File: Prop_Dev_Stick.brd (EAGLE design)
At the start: 63.2 x 24.9 mm, 55 parts, among them J1 MF-CON-MICROUSB-RIGHT, J3 M20-7822046, J4 M20-7822046, J5 M20-7820442, J6 M20-7820442, U1 P8X32A-Q44, U2 FT230XQ-R, U3 TPS2113ADRBR, U4 CAT24C512WI-GT3, U5 MAX11613EUA+, U6 NCP1117LPST33T3G, U7 IRLML6401TRPBF, X1 ABMM-6.000MHZ-B2-T

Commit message: Updated design to use latest library style!
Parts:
- removed J6: M20-7820442, PP_Connectors:HEADER_01X04_PTH_ROUND
- added J2: (no value), PP_Connectors:2.54MM_01X04_PIN_HEADER
- J1: device MF_Connectors:MICROUSB-RIGHT -> PP_Connectors:10118193-0001LF
- J3: value M20-7822046 -> (none); device PP_Connectors:HEADER_01X20_PTH_ROUND -> PP_Connectors:2.54MM_01X04_PIN_HEADER
- J4: device PP_Connectors:HEADER_01X20_PTH_ROUND -> PP_Connectors:2.54MM_01X20_PIN_HEADER
- J5: value M20-7820442 -> M20-7822046; device PP_Connectors:HEADER_01X04_PTH_ROUND -> PP_Connectors:2.54MM_01X20_PIN_HEADER
- U1: device PP_DigitalIC:LQFP-44 -> PP_DigitalIC:P8X32A_LQFP-44
- U2: device PP_DigitalIC:QFN-16 -> PP_DigitalIC:FT230X_QFN-16
- U3: device PP_PowerIC:SON-8 -> PP_PowerIC:TPS211X_SON-8
- U5: device PP_AnalogIC:UMAX-8 -> PP_AnalogIC:MAX11613_UMAX-8
- U7: device PP_DiscreteSemi:SOT-23 -> PP_DiscreteSemi:SOT-23-3
- moved J3 40.2 mm to (58.2, 23.9)
- moved J5 33.0 mm to (25.1, 23.9)
- moved J4 22.9 mm to (25.1, 1.02)
- moved J1 1.27 mm to (1.52, 12.4)
- turned U4 to 0 degrees
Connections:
- net 3.3V: now also J2.2, J3.2, J5.3; no longer J3.3, J5.2, J6.2
- net A0: now also J2.3; no longer J6.3
- net A1: now also J2.4; no longer J6.4
- net A2: now also J3.3; no longer J5.3
- net A3: now also J3.4; no longer J5.4
- net GND: now also J2.1, J3.1, J5.4, U3.PAD, U4.1; no longer J1.S5, J1.S6, J3.4, J5.1, J6.1
- net P10: now also J4.15; no longer J3.15
- net P11: now also J4.16; no longer J3.16
- net P12: now also J4.17; no longer J3.17
- net P13: now also J4.18; no longer J3.18
- net P14: now also J4.19; no longer J3.19
- net P15: now also J4.20; no longer J3.20
- net P16: now also J5.20; no longer J4.20
- net P17: now also J5.19; no longer J4.19
- net P18: now also J5.18; no longer J4.18
- net P19: now also J5.17; no longer J4.17
- net P20: now also J5.16; no longer J4.16
- net P21: now also J5.15; no longer J4.15
- net P22: now also J5.14; no longer J4.14
- net P23: now also J5.13; no longer J4.13
- net P24: now also J5.12; no longer J4.12
- net P25: now also J5.11; no longer J4.11
- net P26: now also J5.10; no longer J4.10
- net P27: now also J5.9; no longer J4.9
- net P4: now also J4.9; no longer J3.9
- net P5: now also J4.10; no longer J3.10
- net P6: now also J4.11; no longer J3.11
- net P7: now also J4.12; no longer J3.12
- net P8: now also J4.13; no longer J3.13
- net P9: now also J4.14; no longer J3.14
- net RX: now also J5.6; no longer J4.6
- net SCL: now also J5.8; no longer J4.8
- net SDA: now also J5.7; no longer J4.7
- net SD_CS: now also J4.5; no longer J3.5
- net SD_DI: now also J4.6; no longer J3.6
- net SD_DO: now also J4.8; no longer J3.8
- net SD_SCLK: now also J4.7; no longer J3.7
- net TX: now also J5.5; no longer J4.5
- net VBUS_P2: now also J5.2; no longer J3.2
- net VIN: now also J5.1; no longer J3.1
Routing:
- net GND: track 7.92 -> 10.3 mm, vias 36 -> 35
- net VBUS_P2: track 50.1 -> 49.0 mm
- net 3.3V: track 209.7 -> 210.2 mm
- net VIN: track 50.1 -> 49.6 mm

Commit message: REV 4B
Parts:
- J1: device PP_Connectors:10118193-0001LF -> MF_Connectors:MICROUSB-RIGHT
- moved J1 1.27 mm to (2.79, 12.4)
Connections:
- net GND: now also J1.S5, J1.S6
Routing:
- net GND: track 10.3 -> 18.9 mm
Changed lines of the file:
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@@
 <layer number="122" name="_bsilk" color="7" fill="1" visible="no" active="yes"/>
 <layer number="125" name="_tNames" color="7" fill="1" visible="no" active="yes"/>
+<layer number="128" name="128bmp" color="1" fill="10" visible="yes" active="yes"/>
+<layer number="129" name="129bmp" color="2" fill="4" visible="yes" active="yes"/>
+<layer number="130" name="130bmp" color="2" fill="1" visible="yes" active="yes"/>
 <layer number="131" name="prix" color="7" fill="1" visible="yes" active="yes"/>
 <layer number="132" name="test" color="7" fill="1" visible="yes" active="yes"/>
@@
 <attribute name="NAME" x="47.25225" y="19.807" size="0.8128" layer="21" font="vector"/>
 </element>
-<element name="J1" library="PP_Connectors" package="10118193-0001LF" value="MF-CON-MICROUSB-RIGHT" x="1.524" y="12.446" smashed="yes" rot="R270">
-<attribute name="NAME" x="0.635" y="17.686" size="0.8128" layer="25" font="vector"/>
-</element>
 <element name="X1" library="MF_Frequency_Control" package="7MMX5MM" value="ABMM-6.000MHZ-B2-T" x="28.829" y="18.923" smashed="yes" rot="MR0">
 <attribute name="NAME" x="32.429" y="21.923" size="0.8128" layer="26" font="vector" rot="MR0"/>
@@
 <attribute name="LABEL04" value="" x="61.976" y="-1.524" size="0.8128" layer="21" font="vector" ratio="16" rot="R90" align="center-right"/>
 <attribute name="LABEL01" value="" x="54.356" y="-1.524" size="0.8128" layer="21" font="vector" ratio="16" rot="R90" align="center-right"/>
-<attribute name="NAME" x="51.562" y="1.8415" size="0.8128" layer="21" font="vector" ratio="16"/>
 </element>
 <element name="J3" library="PP_Connectors" package="2.54MM_01X04_PIN_HEADER" value="" x="58.166" y="23.876" smashed="yes">
@@
 <attribute name="LABEL04" value="" x="61.976" y="21.336" size="0.8128" layer="21" font="vector" ratio="16" rot="R90" align="center-right"/>
 <attribute name="LABEL01" value="" x="54.356" y="21.336" size="0.8128" layer="21" font="vector" ratio="16" rot="R90" align="center-right"/>
-<attribute name="NAME" x="51.308" y="22.4155" size="0.8128" layer="21" font="vector" ratio="16"/>
 </element>
 <element name="J4" library="PP_Connectors" package="2.54MM_01X20_PIN_HEADER" value="M20-7822046" x="25.146" y="1.016" smashed="yes">
@@
 <attribute name="LABEL01" value="" x="1.016" y="-1.524" size="0.8128" layer="21" font="vector" ratio="16" rot="R90" align="center-right"/>
 <attribute name="LABEL02" value="" x="3.556" y="-1.524" size="0.8128" layer="21" font="vector" ratio="16" rot="R90" align="center-right"/>
-<attribute name="NAME" x="39.624" y="3.3655" size="0.8128" layer="21" font="vector" ratio="16"/>
 </element>
 <element name="J5" library="PP_Connectors" package="2.54MM_01X20_PIN_HEADER" value="M20-7822046" x="25.146" y="23.876" smashed="yes">
@@
 <attribute name="LABEL01" value="" x="1.016" y="21.336" size="0.8128" layer="21" font="vector" ratio="16" rot="R90" align="center-right"/>
 <attribute name="LABEL02" value="" x="3.556" y="21.336" size="0.8128" layer="21" font="vector" ratio="16" rot="R90" align="center-right"/>
-<attribute name="NAME" x="22.606" y="20.3835" size="0.8128" layer="21" font="vector" ratio="16"/>
+</element>
+<element name="J1" library="MF_Connectors" package="MICROUSB-RIGHT" value="MF-CON-MICROUSB-RIGHT" x="2.794" y="12.446" smashed="yes" rot="R270">
+<attribute name="NAME" x="0.67" y="17.686" size="0.8128" layer="25" font="vector"/>
 </element>
 </elements>
@@
 <via x="52.07" y="7.112" extent="1-16" drill="0.5"/>
 <via x="52.07" y="5.588" extent="1-16" drill="0.5"/>
-<contactref element="J1" pad="5"/>
-<contactref element="J1" pad="5"/>
-<contactref element="J1" pad="S1"/>
-<contactref element="J1" pad="S4"/>
-<contactref element="J1" pad="S3"/>
-<contactref element="J1" pad="S2"/>
 <via x="18.288" y="14.478" extent="1-16" drill="0.5"/>
 <via x="23.622" y="18.034" extent="1-16" drill="0.5"/>
@@
 <contactref element="J4" pad="4"/>
 <contactref element="J5" pad="4"/>
+<contactref element="J1" pad="5"/>
+<contactref element="J1" pad="S1"/>
+<contactref element="J1" pad="S3"/>
+<contactref element="J1" pad="S5"/>
+<contactref element="J1" pad="S2"/>
+<contactref element="J1" pad="S4"/>
+<contactref element="J1" pad="S6"/>
+<wire x1="1.389" y1="13.646" x2="1.27" y2="13.646" width="0.6096" layer="1"/>
+<wire x1="1.27" y1="13.646" x2="1.27" y2="15.746" width="0.6096" layer="1"/>
+<wire x1="1.27" y1="15.746" x2="1.27" y2="17.018" width="0.6096" layer="1"/>
+<wire x1="1.389" y1="11.246" x2="1.27" y2="11.246" width="0.6096" layer="1"/>
+<wire x1="1.27" y1="11.246" x2="1.27" y2="9.146" width="0.6096" layer="1"/>
+<wire x1="1.27" y1="7.874" x2="1.394" y2="7.874" width="0.6096" layer="1"/>
+<wire x1="1.394" y1="7.874" x2="1.394" y2="9.146" width="0.6096" layer="1"/>
+<wire x1="1.394" y1="15.746" x2="1.27" y2="15.746" width="0.6096" layer="1"/>
+<wire x1="1.394" y1="9.146" x2="1.27" y2="9.146" width="0.6096" layer="1"/>
+<wire x1="1.27" y1="9.146" x2="1.27" y2="7.874" width="0.6096" layer="1"/>
 </signal>
 <signal name="SDA">
@@
 <signal name="VBUS">
 <contactref element="L1" pad="1"/>
-<contactref element="J1" pad="1"/>
-<wire x1="4.064" y1="13.746" x2="4.856" y2="13.746" width="0.254" layer="1"/>
 <wire x1="4.856" y1="13.746" x2="5.969" y2="14.859" width="0.254" layer="1"/>
 <wire x1="5.969" y1="14.859" x2="6.008" y2="14.859" width="0.254" layer="1"/>
+<contactref element="J1" pad="1"/>
+<wire x1="4.856" y1="13.746" x2="4.064" y2="13.746" width="0.254" layer="1"/>
 </signal>
 <signal name="D+">
@@
 <wire x1="5.246" y1="12.446" x2="6.008" y2="11.684" width="0.254" layer="1"/>
 <contactref element="J1" pad="3"/>
-<wire x1="4.064" y1="12.446" x2="5.246" y2="12.446" width="0.254" layer="1"/>
+<wire x1="5.246" y1="12.446" x2="4.064" y2="12.446" width="0.254" layer="1"/>
 </signal>
 <signal name="RX">
@@
 <contactref element="R13" pad="2"/>
 <wire x1="6.008" y1="12.969" x2="6.008" y2="13.208" width="0.254" layer="1"/>
+<wire x1="5.896" y1="13.096" x2="6.008" y2="13.208" width="0.254" layer="1"/>
 <contactref element="J1" pad="2"/>
-<wire x1="4.064" y1="13.096" x2="5.896" y2="13.096" width="0.254" layer="1"/>
-<wire x1="5.896" y1="13.096" x2="6.008" y2="13.208" width="0.254" layer="1"/>
+<wire x1="5.896" y1="13.096" x2="4.064" y2="13.096" width="0.254" layer="1"/>
 </signal>
 <signal name="5V">

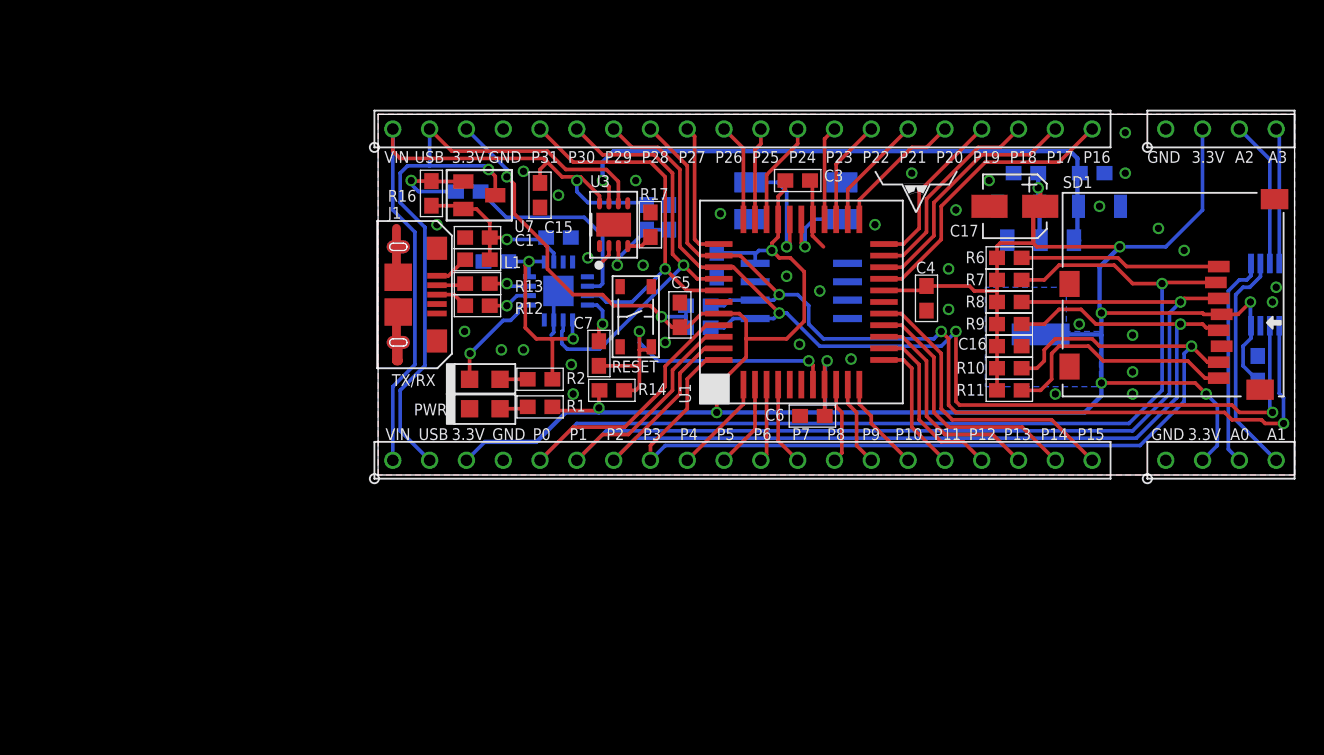
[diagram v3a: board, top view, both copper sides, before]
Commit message: Working on REV5
REV5 will feature 0402 parts, QFN Prop, USB Type-C, and a host of other
small changes.
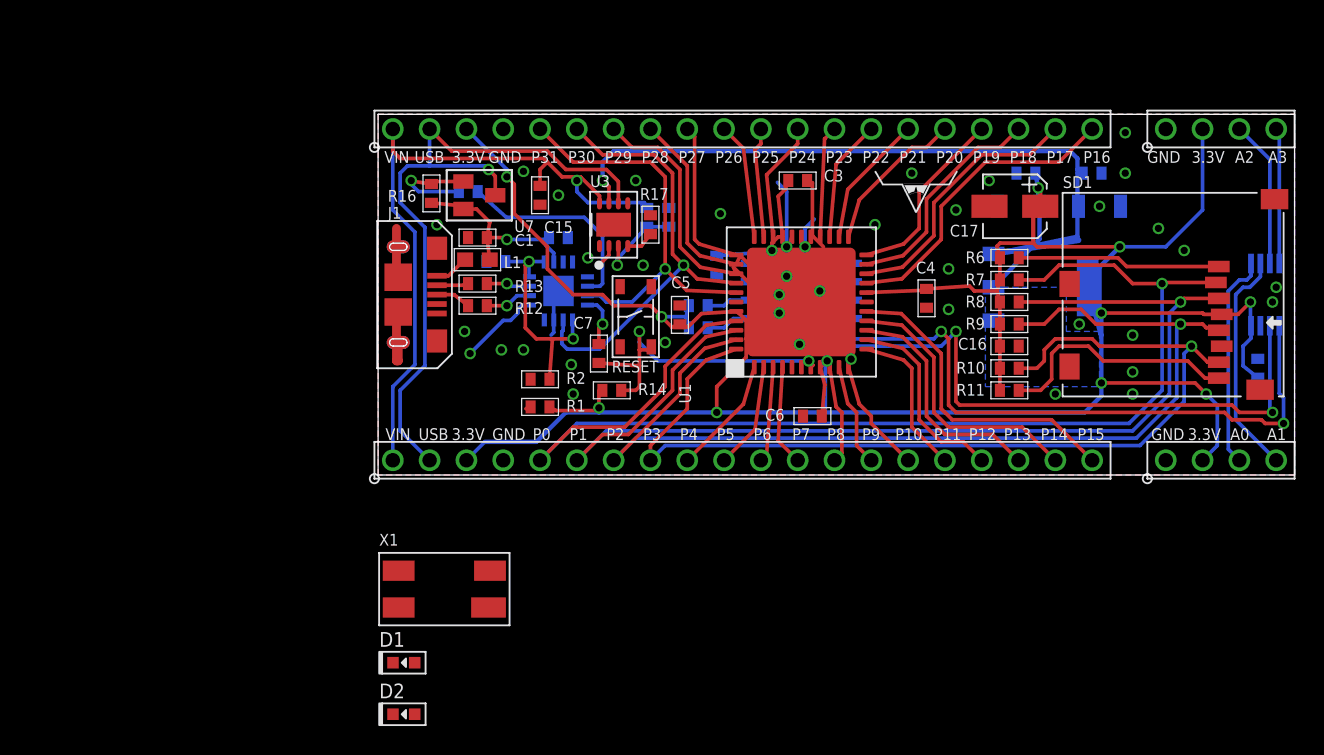
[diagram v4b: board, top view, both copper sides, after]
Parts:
- removed PWR, TX/RX: 598-8020-107F, PP_LED:LED_0805
- added D1: MF-LED-0603-GREEN, MF_LEDs:LED0603
- added D2: MF-LED-0603-RED, MF_LEDs:LED0603
- C1, C10, C11, C12, C13, C14, C15, C16, C2, C3, C4, C5, C6, C7, R1, R10, R11, R12, R13, R14, R15, R16, R17, R18, R2, R3, R4, R5, R6, R7, R8, R9: device PP_Passives:0603 -> PP_Passives:0402
- J4, J5: value M20-7822046 -> (none)
- SD1: value MF-CON-MICROSDSLOT-RIGHT -> MF-MICROSD; device MF_Connectors:MICROSDSLOT-RIGHT -> MF_Connectors:MF-MICROSD
- U1: value P8X32A-Q44 -> P8X32A-M44; device PP_DigitalIC:P8X32A_LQFP-44 -> PP_DigitalIC:P8X32A_QFN-44
- X1: device MF_Frequency_Control:7MMX5MM -> PP_FreqCtrl:7MM_X_5MM
- moved X1 36.1 mm to (4.57, -7.87), flipped to the top
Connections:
- net GND: now also D1.CATHODE, X1.2, X1.4; no longer PWR.CATHODE, X1.P$2, X1.P$4
- net N$1: now also D1.ANODE; no longer PWR.ANODE
- net N$2: now also D2.ANODE; no longer TX/RX.ANODE
- net TX_RX_LED: now also D2.CATHODE; no longer TX/RX.CATHODE
- net X0: now also X1.3; no longer X1.P$3
- net X1: now also X1.1; no longer X1.P$1
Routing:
- net 5V: track 43.0 -> 54.4 mm
- net 3.3V: track 210.2 -> 216.1 mm
- net X1: track 6.04 -> 2.96 mm
- net X0: track 8.57 -> 5.51 mm
- net N$2: track 1.91 -> 0.00 mm
- net TX_RX_LED: track 7.42 -> 5.68 mm
- net N$1: track 1.96 -> 0.35 mm
- net SD_DO: track 67.5 -> 69.0 mm
- net SD_SCLK: track 72.0 -> 73.4 mm
- net SD_DI: track 77.3 -> 78.7 mm
- net SD_CS: track 83.7 -> 85.1 mm
- net P20: track 9.28 -> 10.6 mm
- net P4: track 6.83 -> 8.13 mm
- net P27: track 9.63 -> 10.9 mm
- net P10: track 6.62 -> 7.92 mm
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
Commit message: pushing updates from long ago
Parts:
- removed C10, C11, C12, C14, C15, C16, C6, C7: .1uF, PP_Passives:0402
- removed C13: 1uF, PP_Passives:0402
- removed C17: 10uF, MF_Passives:CP4MM
- removed D1: MF-LED-0603-GREEN, MF_LEDs:LED0603
- removed D2: MF-LED-0603-RED, MF_LEDs:LED0603
- removed L1: MI0603K300R-10, PP_Passives:0603
- removed R1, R2: 330, PP_Passives:0402
- removed R10, R11, R14: 10K, PP_Passives:0402
- removed R12: 22, PP_Passives:0402
- removed R17: 1K, PP_Passives:0402
- removed R18: 25K, PP_Passives:0402
- removed R3: 100K, PP_Passives:0402
- removed RESET: MF-SW-TACT-4.2MM, MF_Switches:TACT4.2MM
- removed U6: NCP1117LPST33T3G, MF_IC_Power:SOT-223-3
- removed X1: ABMM-6.000MHZ-B2-T, PP_FreqCtrl:7MM_X_5MM
- added C18, C19: 0.1uF, MF_Passives:C0603
- added C20: 1uF, MF_Passives:C0603
- added C21, C22: 47pF, MF_Passives:C0603
- added C24, C25, C27, C28, C29: 0.1uF, MF_Passives:C0402
- added L3, L4: MI0603K300R-10, MF_Passives:L0603
- added PWR, TXRX1: MF-LED-0603-RED, MF_LEDs:LED0603
- added R24: 5.1K, MF_Passives:R0603
- added R25, R26: 27, MF_Passives:R0603
- added R29, R31: 330, MF_Passives:R0402
- added U8: CAT24C512WI-GT3, PP_DigitalIC:SOIC-8_W
- added X3: ABMM-6.000MHZ-B2-T, MF_Frequency_Control:7MMX5MM
- C1, C2, C3, C4: value .1uF -> 0.1uF; device PP_Passives:0402 -> MF_Passives:C0603
- C5: value .1uF -> 0.1uF; device PP_Passives:0402 -> MF_Passives:C0402
- J1: value MF-CON-MICROUSB-RIGHT -> (none); device MF_Connectors:MICROUSB-RIGHT -> PP_Connectors:105450-0101
- R13: value 22 -> 10K; device PP_Passives:0402 -> MF_Passives:R0402
- R15: value 1K -> 10K; device PP_Passives:0402 -> MF_Passives:R0402
- R16: value 100K -> 10K; device PP_Passives:0402 -> MF_Passives:R0402
- R4, R5, R6, R7, R8, R9: device PP_Passives:0402 -> MF_Passives:R0603
- U1: value P8X32A-M44 -> AP7361C-33ER-13; device PP_DigitalIC:P8X32A_QFN-44 -> PP_PowerIC:ADP3338_SOT-223-3
- U2: value FT230XQ-R -> IP4234CZ6,125; device PP_DigitalIC:FT230X_QFN-16 -> PP_Passives:IP4234CZ6_SOT-457-6
- U3: value TPS2113ADRBR -> BQ24165RGET; device PP_PowerIC:TPS211X_SON-8 -> PP_PowerIC:BQ24165_QFN-24
- U4: value CAT24C512WI-GT3 -> FT230XQ-R; device PP_DigitalIC:SOIC-8_W -> PP_DigitalIC:FT230X_QFN-16
- U7: value IRLML6401TRPBF -> P8X32A-Q44; device PP_DiscreteSemi:SOT-23-3 -> PP_DigitalIC:P8X32A_QFN-44
- moved U$1 60.8 mm to (-18.0, 22.6), flipped to the top
- moved C2 52.4 mm to (60.1, 8.56), turned to 180 degrees
- moved U3 42.0 mm to (-21.6, -1.02)
- moved C1 38.7 mm to (45.2, 11.0)
- moved C8 37.6 mm to (14.0, 6.78), turned to 180 degrees
- moved U$2 28.6 mm to (12.2, 27.8)
- moved R13 26.8 mm to (32.4, 5.13)
- moved U7 26.7 mm to (32.8, 12.4), turned to 90 degrees
- moved C9 25.9 mm to (21.2, 6.58), flipped to the top, turned to 225 degrees
- moved C4 23.9 mm to (15.5, 3.81), flipped to the bottom, turned to 270 degrees
- moved R5 23.4 mm to (45.2, 13.8), flipped to the top, turned to 180 degrees
- moved R4 23.4 mm to (45.2, 15.2), flipped to the top, turned to 180 degrees
- moved C3 18.4 mm to (14.8, 8.59), flipped to the bottom, turned to 0 degrees
- moved R16 15.3 mm to (18.8, 22.0), flipped to the bottom, turned to 90 degrees
- moved U1 10.7 mm to (20.6, 5.59), flipped to the bottom
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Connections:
- removed net 3V3OUT: C2.1, R2.2, U2.1, U2.8, U2.9
- removed net N$41: R15.1, R16.1, U7.1
- removed net N$7: R17.1, U3.4
- removed net PWREN: R15.2, U2.14
- removed net VBUS: J1.1, L1.1
- removed net VBUS_P1: C1.1, C13.1, L1.2, R16.2, U2.10, U7.2
- removed net VBUS_P2: J4.2, J5.2, U3.6, U7.3
- removed net VSNS: R18.2, R3.1, U3.3
- removed net X0: U1.29, X1.3
- removed net X1: U1.28, X1.1
- new net BCD_CHARGER: U4.12
- new net CC1/1: J1.A5, J1.B5, R24.P$1
- new net N$11: J1.S_T1, J1.S_T2, J1.S_T3, J1.S_T4, L4.P$1
- new net N$16: C21.P$1, R26.P$1, U2.1
- new net N$17: C22.P$1, R25.P$1, U2.6
- new net N$3: PWR.CATHODE, R31.P$1
- new net USB_VBUS: C18.P$1, C20.P$1, L3.P$2, TXRX1.ANODE, U2.5
- new net USB_VBUS_PORT: J1.A4, J1.A9, J1.B4, J1.B9, L3.P$1
- new net X4: U7.29, X3.P$3
- new net X5: U7.28, X3.P$1
- net 3.3V: now also C1.P$1, C19.P$1, C2.P$1, C24.P$1, C25.P$1, C27.P$1, C28.P$1, C29.P$1, C4.P$1, R13.P$1, R15.P$1, R16.P$1, R4.P$2, R5.P$2, R6.P$2, R7.P$2, R8.P$2, R9.P$2, U1.2, U1.PAD, U4.1, U4.10, U4.9, U7.18, U7.30, U7.40, U7.8, U8.8; no longer C11.1, C12.2, C14.1, C16.1, C17.P$1, C3.2, C4.2, C5.2, C6.2, R1.2, R10.2, R11.2, R14.2, R4.2, R5.2, R6.2, R7.2, R8.2, R9.2, U1.18, U1.30, U1.40, U1.8, U6.P$1, U6.P$3
- net 5V: now also C3.P$1, J4.2, J5.2, PWR.ANODE, U1.3; no longer C10.1, U3.7, U6.P$4
- net D+: now also J1.A6, J1.B6, U2.3; no longer J1.3, R12.2
- net D-: now also J1.A7, J1.B7, U2.4; no longer J1.2, R13.2
- net GND: now also C1.P$2, C18.P$2, C19.P$2, C2.P$2, C20.P$2, C21.P$2, C22.P$2, C24.P$2, C25.P$2, C27.P$2, C28.P$2, C29.P$2, C3.P$2, C4.P$2, J1.A1, J1.A12, J1.B1, J1.B12, L4.P$2, R24.P$2, R31.P$2, U1.1, U2.2, U4.13, U4.PAD, U7.17, U7.27, U7.39, U7.5, U7.6, U8.1, U8.2, U8.3, U8.4, U8.7, X3.P$2, X3.P$4; no longer C1.2, C10.2, C11.2, C12.1, C13.2, C14.2, C15.1, C16.2, C17.P$2, C2.2, C3.1, C4.1, C5.1, C6.1, D1.CATHODE, J1.5, J1.S1, J1.S2, J1.S3, J1.S4, J1.S5, J1.S6, R17.2, R18.1, RESET.P$3, RESET.P$4, U1.17, U1.27, U1.39, U1.5, U1.6, U2.13, U2.3, U2.PAD, U3.2, U3.5, U3.PAD, U4.1, U4.2, U4.4, U4.7, U6.P$2, X1.2, X1.4
- net IRQ: now also R9.P$1; no longer R11.1
- net N$1: now also U4.14; no longer D1.ANODE, R1.1
- net N$2: now also R29.P$1, TXRX1.CATHODE; no longer D2.ANODE, R2.1
- net P10: now also U7.11; no longer U1.11
- net P11: now also U7.12; no longer U1.12
- net P12: now also U7.13; no longer U1.13
- net P13: now also U7.14; no longer U1.14
- net P14: now also U7.15; no longer U1.15
- net P15: now also U7.16; no longer U1.16
- net P16: now also U7.19; no longer U1.19
- net P17: now also U7.20; no longer U1.20
- net P18: now also U7.21; no longer U1.21
- net P19: now also U7.22; no longer U1.22
- net P20: now also U7.23; no longer U1.23
- net P21: now also U7.24; no longer U1.24
- net P22: now also U7.25; no longer U1.25
- net P23: now also U7.26; no longer U1.26
- net P24: now also U7.31; no longer U1.31
- net P25: now also U7.32; no longer U1.32
- net P26: now also U7.33; no longer U1.33
- net P27: now also U7.34; no longer U1.34
- net P4: now also U7.1; no longer U1.1
- net P5: now also U7.2; no longer U1.2
- net P6: now also U7.3; no longer U1.3
- net P7: now also U7.4; no longer U1.4
- net P8: now also U7.9; no longer U1.9
- net P9: now also U7.10; no longer U1.10
- net RES: now also C5.P$1, R13.P$2, U7.7; no longer C7.2, R14.1, RESET.P$2, U1.7
- net RTS: now also C5.P$2, U4.16; no longer C7.1, U2.16
- net RW: now also R4.P$1; no longer R6.1
- net RX: now also U4.2, U7.37; no longer U1.37, U2.2
- net SCL: now also R16.P$2, U7.35, U8.6; no longer R4.1, U1.35, U4.6
- net SDA: now also R15.P$2, U7.36, U8.5; no longer R5.1, U1.36, U4.5
- net SD_CS: now also R5.P$1, U7.41; no longer R7.1, U1.41
- net SD_DI: now also R6.P$1, U7.42; no longer R8.1, U1.42
- net SD_DO: now also R8.P$1, U7.44; no longer R10.1, U1.44
- net SD_SCLK: now also R7.P$1, U7.43; no longer R9.1, U1.43
- net TX: now also U4.15, U7.38; no longer U1.38, U2.15
- net TX_RX_LED: now also R29.P$2, U4.5; no longer D2.CATHODE, U2.5
- net USBDM: now also R25.P$2, U4.7; no longer R13.1, U2.7
- net USBDP: now also R26.P$2, U4.6; no longer R12.1, U2.6
- net VIN: no longer C15.2, R3.2, U3.8
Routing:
- net 3.3V: track 216.1 -> 28.9 mm, vias 12 -> 17
- net VBUS_P2: track 49.0 -> 0.00 mm, vias 1 -> 0
- net USB_VBUS: track 0.00 -> 45.1 mm
- net GND: track 19.1 -> 54.8 mm, vias 35 -> 34
- net SD_CS: track 85.1 -> 64.7 mm, vias 1 -> 2
- net SD_DI: track 78.7 -> 60.8 mm, vias 1 -> 2
- net SD_SCLK: track 73.4 -> 57.1 mm, vias 1 -> 2
- net 3V3OUT: track 16.2 -> 0.00 mm, vias 2 -> 0
- net PWREN: track 14.3 -> 0.00 mm
- net SD_DO: track 69.0 -> 55.6 mm, vias 1 -> 2
- net VBUS_P1: track 13.4 -> 0.00 mm, vias 1 -> 0
- net VIN: track 49.9 -> 38.8 mm, vias 1 -> 0
- net USB_VBUS_PORT: track 0.00 -> 10.7 mm
- net TX_RX_LED: track 5.68 -> 15.9 mm, vias 1 -> 0
- net CC1/1: track 0.00 -> 8.48 mm, vias 0 -> 2
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- added copper zone on layer 15, net 3.3V
- added copper zone on layer 2, net GND
- removed copper zone on layer 1, net GND
- removed copper zone on layer 16, net GND
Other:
- board text removed: "3.3V"
- board text removed: "A0"
- board text removed: "A1"
- board text removed: "A2"
- board text removed: "A3"
- board text removed: "GND"
- board text removed: "P0"
- board text removed: "P1"
- board text removed: "P10"
- board text removed: "P11"
- board text removed: "P12"
- board text removed: "P13"
- board text removed: "P14"
- board text removed: "P15"
- board text removed: "P16"
- board text removed: "P17"
- board text removed: "P18"
- board text removed: "P19"
- board text removed: "P2"
- board text removed: "P20"
- board text removed: "P21"
- board text removed: "P22"
- board text removed: "P23"
- board text removed: "P24"
- board text removed: "P25"
- board text removed: "P26"
- board text removed: "P27"
- board text removed: "P28"
- board text removed: "P29"
- board text removed: "P3"
- board text removed: "P30"
- board text removed: "P31"
- board text removed: "P4"
- board text removed: "P5"
- board text removed: "P6"
- board text removed: "P7"
- board text removed: "P8"
- board text removed: "P9"
- board text removed: "USB"
- board text removed: "VIN"
